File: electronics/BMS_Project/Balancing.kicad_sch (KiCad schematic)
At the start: 20 parts, among them Q1 IRLB8721PBF, Q2 IRLB8721PBF, Q3 IRLB8721PBF, Q4 IRLB8721PBF, U3 LTV-817, U4 LTV-817, U5 LTV-817, U6 LTV-817

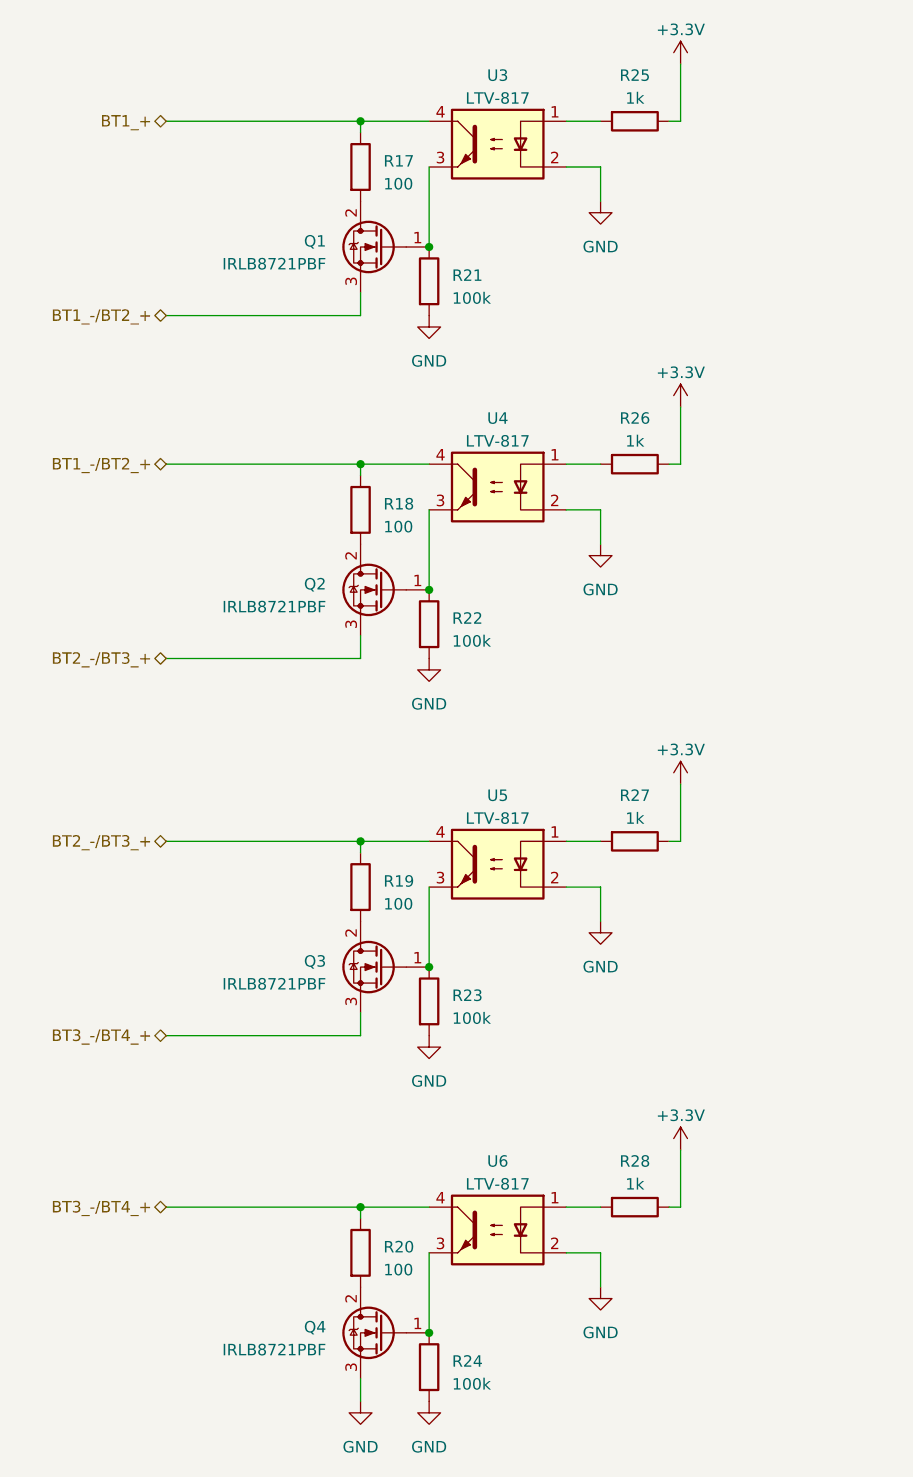
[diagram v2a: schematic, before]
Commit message: small tweaks to the labels
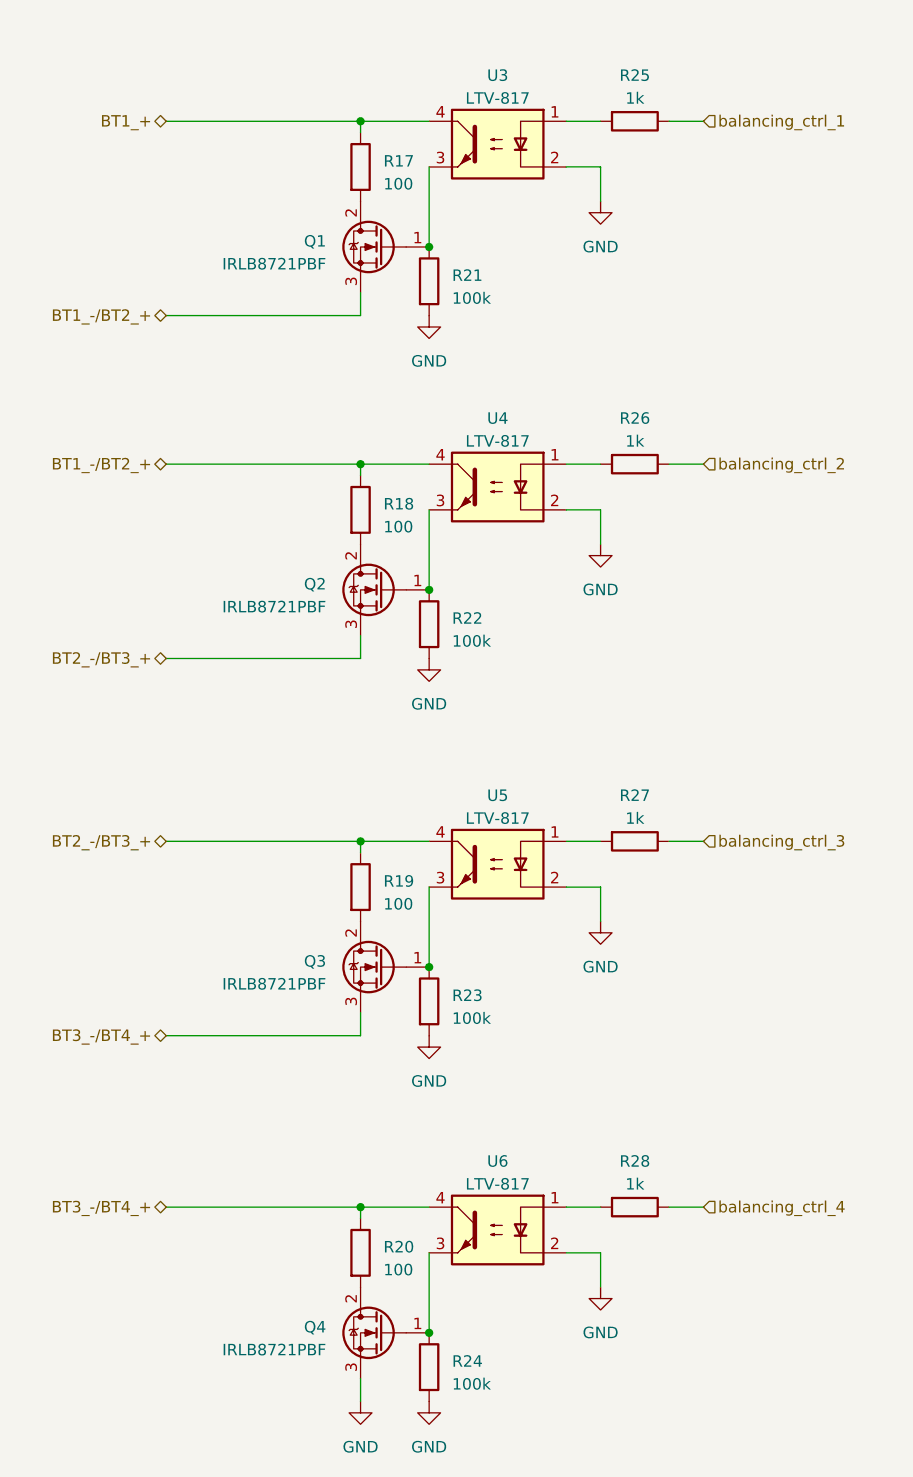
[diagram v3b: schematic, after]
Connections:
- removed net +3.3V: R25.1, R26.1, R27.1, R28.1
- new net balancing_ctrl_1: R25.1
- new net balancing_ctrl_2: R26.1
- new net balancing_ctrl_3: R27.1
- new net balancing_ctrl_4: R28.1
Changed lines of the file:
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@@
-    (stroke (width 0) (type default))
-  )
-  (wire (pts (xy 148.59 152.4) (xy 149.86 152.4))
-    (stroke (width 0) (type default))
-  )
-  (wire (pts (xy 148.59 31.75) (xy 149.86 31.75))
-    (stroke (width 0) (type default))
-  )
-  (wire (pts (xy 149.86 31.75) (xy 149.86 25.4))
     (stroke (width 0) (type default))
   )
@@
     (stroke (width 0) (type default))
   )
-  (wire (pts (xy 149.86 69.85) (xy 149.86 63.5))
+  (wire (pts (xy 148.59 31.75) (xy 152.4 31.75))
     (stroke (width 0) (type default))
   )
@@
     (stroke (width 0) (type default))
   )
-  (wire (pts (xy 149.86 111.76) (xy 149.86 105.41))
-    (stroke (width 0) (type default))
-  )
   (wire (pts (xy 92.71 69.85) (xy 114.3 69.85))
     (stroke (width 0) (type default))
@@
     (stroke (width 0) (type default))
   )
-  (wire (pts (xy 149.86 152.4) (xy 149.86 146.05))
-    (stroke (width 0) (type default))
-  )
   (wire (pts (xy 121.92 157.48) (xy 121.92 166.37))
     (stroke (width 0) (type default))
@@
     (stroke (width 0) (type default))
   )
-  (wire (pts (xy 148.59 111.76) (xy 149.86 111.76))
+  (wire (pts (xy 148.59 111.76) (xy 152.4 111.76))
     (stroke (width 0) (type default))
   )
@@
     (stroke (width 0) (type default))
   )
-  (wire (pts (xy 148.59 69.85) (xy 149.86 69.85))
+  (wire (pts (xy 148.59 69.85) (xy 152.4 69.85))
     (stroke (width 0) (type default))
   )
@@
   (wire (pts (xy 137.16 157.48) (xy 140.97 157.48))
     (stroke (width 0) (type default))
+  )
+  (wire (pts (xy 148.59 152.4) (xy 152.4 152.4))
+    (stroke (width 0) (type default))
+  )
+  (hierarchical_label "balancing_ctrl_1" (shape input) (at 152.4 31.75 0) (fields_autoplaced)
+    (effects (font (size 1.27 1.27)) (justify left))
   )
   (hierarchical_label "BT1_-{slash}BT2_+" (shape bidirectional) (at 92.71 53.34 180) (fields_autoplaced)
@@
     (effects (font (size 1.27 1.27)) (justify right))
   )
+  (hierarchical_label "balancing_ctrl_3" (shape input) (at 152.4 111.76 0) (fields_autoplaced)
+    (effects (font (size 1.27 1.27)) (justify left))
+  )
   (hierarchical_label "BT3_-{slash}BT4_+" (shape bidirectional) (at 92.71 133.35 180) (fields_autoplaced)
     (effects (font (size 1.27 1.27)) (justify right))
@@
   (hierarchical_label "BT2_-{slash}BT3_+" (shape bidirectional) (at 92.71 111.76 180) (fields_autoplaced)
     (effects (font (size 1.27 1.27)) (justify right))
+  )
+  (hierarchical_label "balancing_ctrl_4" (shape input) (at 152.4 152.4 0) (fields_autoplaced)
+    (effects (font (size 1.27 1.27)) (justify left))
+  )
+  (hierarchical_label "balancing_ctrl_2" (shape input) (at 152.4 69.85 0) (fields_autoplaced)
+    (effects (font (size 1.27 1.27)) (justify left))
   )
   (symbol (lib_id "Device:R") (at 121.92 49.53 0) (unit 1)
@@
     )
   )
-  (symbol (lib_id "power:+3.3V") (at 149.86 63.5 0) (unit 1)
-    (in_bom yes) (on_board yes) (dnp no) (fields_autoplaced)
-    (property "Reference" "#PWR019" (at 149.86 67.31 0)
-      (effects (font (size 1.27 1.27)) hide)
-    )
-    (property "Value" "+3.3V" (at 149.86 59.69 0)
-      (effects (font (size 1.27 1.27)))
-    )
-    (property "Footprint" "" (at 149.86 63.5 0)
-      (effects (font (size 1.27 1.27)) hide)
-    )
-    (property "Datasheet" "" (at 149.86 63.5 0)
-      (effects (font (size 1.27 1.27)) hide)
-    )
-    (pin "1")
-    (instances
-      (project "BMS_Project"
-        (path "/524e7f14-feb0-4ca2-9425-a347c869bfa6/d8f12774-e346-4091-abf5-b4c43e81469c"
-          (reference "#PWR019") (unit 1)
-        )
-        (path "/524e7f14-feb0-4ca2-9425-a347c869bfa6/d60b6f2f-e13e-4849-9977-88b541f58c2b"
-          (reference "#PWR019") (unit 1)
-        )
-      )
-      (project "Test_Projekt"
-        (path "/d5b120ca-a0f0-4b3f-8fab-ca010d94ac2e"
-          (reference "#PWR017") (unit 1)
-        )
-      )
-    )
-  )
   (symbol (lib_id "Device:R") (at 144.78 31.75 270) (unit 1)
     (in_bom yes) (on_board yes) (dnp no) (fields_autoplaced)
@@
     )
   )
-  (symbol (lib_id "power:+3.3V") (at 149.86 105.41 0) (unit 1)
-    (in_bom yes) (on_board yes) (dnp no) (fields_autoplaced)
-    (property "Reference" "#PWR020" (at 149.86 109.22 0)
-      (effects (font (size 1.27 1.27)) hide)
-    )
-    (property "Value" "+3.3V" (at 149.86 101.6 0)
-      (effects (font (size 1.27 1.27)))
-    )
-    (property "Footprint" "" (at 149.86 105.41 0)
-      (effects (font (size 1.27 1.27)) hide)
-    )
-    (property "Datasheet" "" (at 149.86 105.41 0)
-      (effects (font (size 1.27 1.27)) hide)
-    )
-    (pin "1")
-    (instances
-      (project "BMS_Project"
-        (path "/524e7f14-feb0-4ca2-9425-a347c869bfa6/d8f12774-e346-4091-abf5-b4c43e81469c"
-          (reference "#PWR020") (unit 1)
-        )
-        (path "/524e7f14-feb0-4ca2-9425-a347c869bfa6/d60b6f2f-e13e-4849-9977-88b541f58c2b"
-          (reference "#PWR020") (unit 1)
-        )
-      )
-      (project "Test_Projekt"
-        (path "/d5b120ca-a0f0-4b3f-8fab-ca010d94ac2e"
-          (reference "#PWR011") (unit 1)
-        )
-      )
-    )
-  )
   (symbol (lib_id "power:GND") (at 121.92 53.34 0) (unit 1)
     (in_bom yes) (on_board yes) (dnp no) (fields_autoplaced)
@@
     )
   )
-  (symbol (lib_id "power:+3.3V") (at 149.86 146.05 0) (unit 1)
-    (in_bom yes) (on_board yes) (dnp no) (fields_autoplaced)
-    (property "Reference" "#PWR021" (at 149.86 149.86 0)
-      (effects (font (size 1.27 1.27)) hide)
-    )
-    (property "Value" "+3.3V" (at 149.86 142.24 0)
-      (effects (font (size 1.27 1.27)))
-    )
-    (property "Footprint" "" (at 149.86 146.05 0)
-      (effects (font (size 1.27 1.27)) hide)
-    )
-    (property "Datasheet" "" (at 149.86 146.05 0)
-      (effects (font (size 1.27 1.27)) hide)
-    )
-    (pin "1")
-    (instances
-      (project "BMS_Project"
-        (path "/524e7f14-feb0-4ca2-9425-a347c869bfa6/d8f12774-e346-4091-abf5-b4c43e81469c"
-          (reference "#PWR021") (unit 1)
-        )
-        (path "/524e7f14-feb0-4ca2-9425-a347c869bfa6/d60b6f2f-e13e-4849-9977-88b541f58c2b"
-          (reference "#PWR021") (unit 1)
-        )
-      )
-      (project "Test_Projekt"
-        (path "/d5b120ca-a0f0-4b3f-8fab-ca010d94ac2e"
-          (reference "#PWR04") (unit 1)
-        )
-      )
-    )
-  )
   (symbol (lib_id "Device:R") (at 144.78 111.76 270) (unit 1)
     (in_bom yes) (on_board yes) (dnp no) (fields_autoplaced)
@@
         )
       )
-    )
-  )
-  (symbol (lib_id "power:+3.3V") (at 149.86 25.4 0) (unit 1)
-    (in_bom yes) (on_board yes) (dnp no) (fields_autoplaced)
-    (property "Reference" "#PWR018" (at 149.86 29.21 0)
-      (effects (font (size 1.27 1.27)) hide)
-    )
-    (property "Value" "+3.3V" (at 149.86 21.59 0)
-      (effects (font (size 1.27 1.27)))
-    )
-    (property "Footprint" "" (at 149.86 25.4 0)
-      (effects (font (size 1.27 1.27)) hide)
-    )
-    (property "Datasheet" "" (at 149.86 25.4 0)
-      (effects (font (size 1.27 1.27)) hide)
-    )
-    (pin "1")
-    (instances
-      (project "BMS_Project"
-        (path "/524e7f14-feb0-4ca2-9425-a347c869bfa6/d8f12774-e346-4091-abf5-b4c43e81469c"
-          (reference "#PWR018") (unit 1)
-        )
-        (path "/524e7f14-feb0-4ca2-9425-a347c869bfa6/d60b6f2f-e13e-4849-9977-88b541f58c2b"
-          (reference "#PWR018") (unit 1)
-        )
-      )
-      (project "Test_Projekt"
-        (path "/d5b120ca-a0f0-4b3f-8fab-ca010d94ac2e"
-          (reference "#PWR024") (unit 1)
-        )
-      )
